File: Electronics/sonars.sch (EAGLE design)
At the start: 6 parts, among them X1 GLX-S-88M

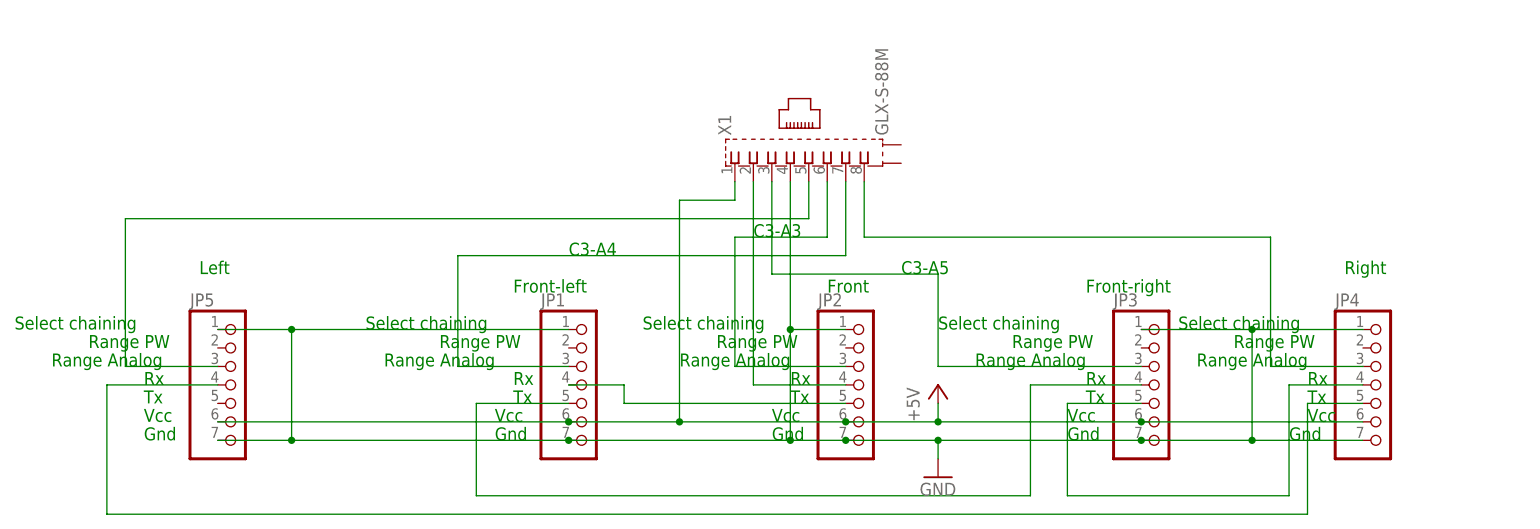
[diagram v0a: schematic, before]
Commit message: Parts match physical size
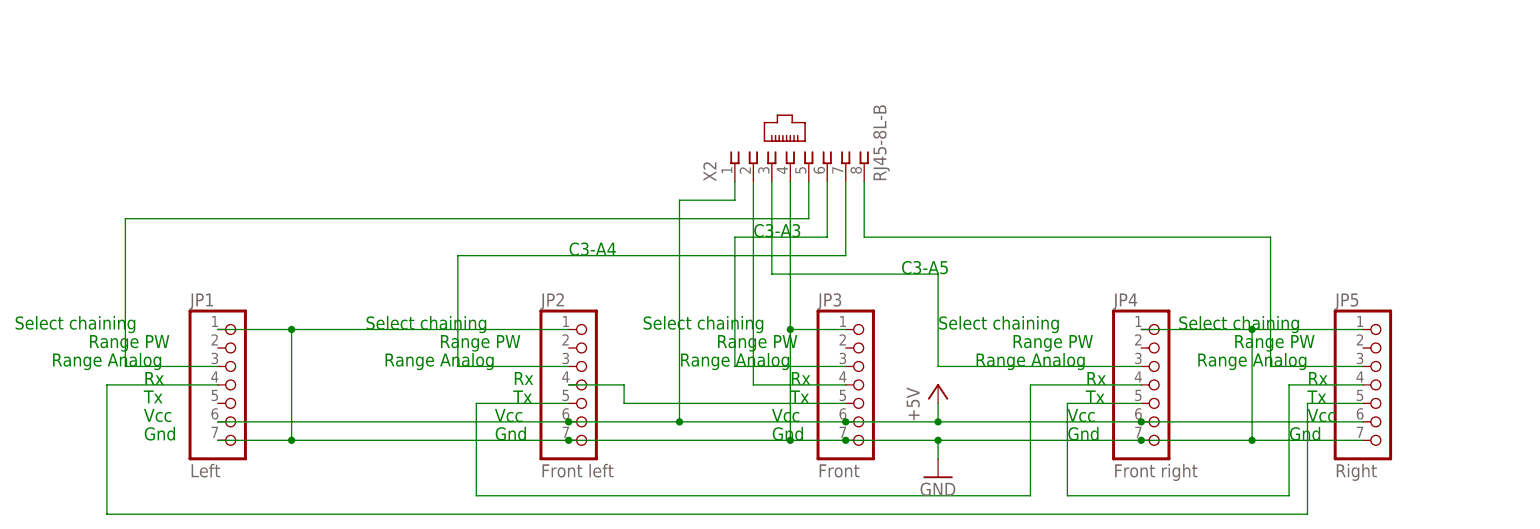
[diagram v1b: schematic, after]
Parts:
- removed X1: GLX-S-88M, con-kycon:GLX-S-88M
- added X2: RJ45-8L-B, con-tycoelectronics:RJ45-8L-B
- JP1: value (none) -> Left
- JP2: value (none) -> Front left
- JP3: value (none) -> Front
- JP4: value (none) -> Front right
- JP5: value (none) -> Right
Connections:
- net N$10 renamed FR>R
- removed net N$1: JP2.3, X1.6
- removed net N$11: JP4.3, X1.8
- removed net N$12: JP5.3, X1.5
- removed net N$2: JP1.3, X1.7
- removed net N$3: JP3.3, X1.3
- removed net N$5: JP2.4, X1.2
- removed net N$7: JP1.4, JP2.5
- removed net N$8: JP1.5, JP3.4
- removed net N$9: JP3.5, JP4.4
- new net CHN: JP3.4, X2.2
- new net F: JP3.3, X2.6
- new net F>FL: JP2.4, JP3.5
- new net FL: JP2.3, X2.7
- new net FL>FR: JP2.5, JP4.4
- new net FR: JP4.3, X2.3
- new net L: JP1.3, X2.5
- new net R: JP5.3, X2.8
- new net R>L: JP1.4, JP5.5
- net +5V: now also X2.1; no longer X1.1
- net GND: now also X2.4; no longer X1.4
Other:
- note removed: "Front"
- note removed: "Front-left"
- note removed: "Front-right"
- note removed: "Left"
- note removed: "Right"
- moved on the sheet: JP1, JP2, JP3, JP4, JP5

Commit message: Rear facing sonars; angles adjusted
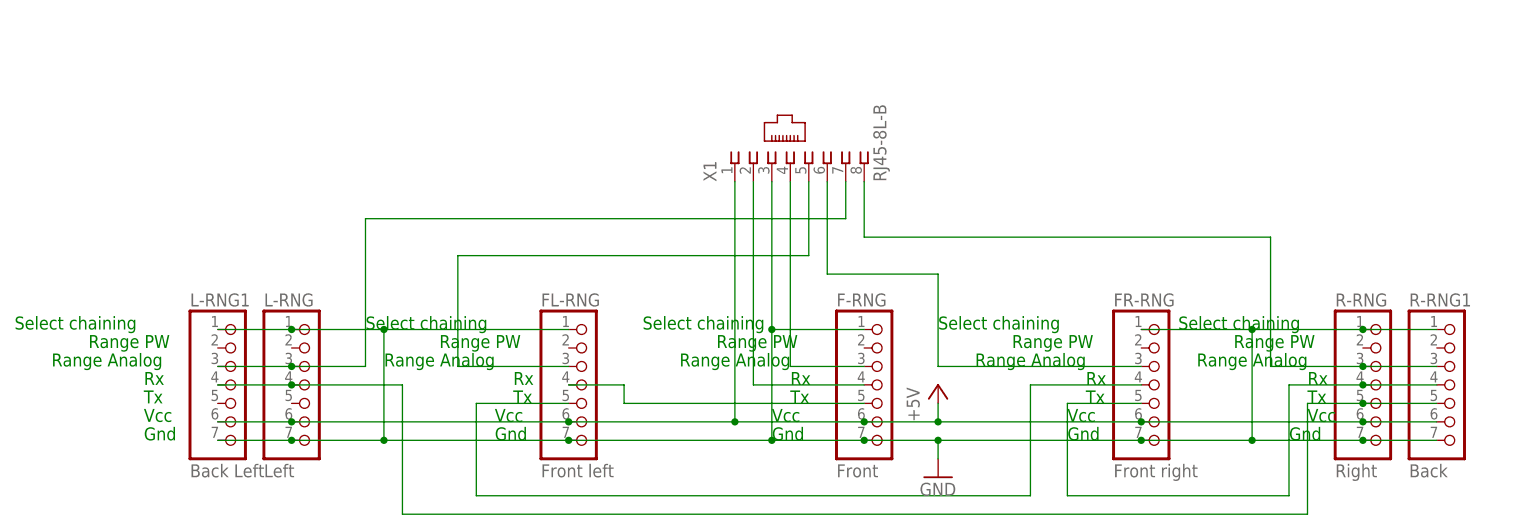
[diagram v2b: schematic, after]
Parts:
- removed JP3: Front, pinhead:PINHD-1X7
- added F-RNG: Front, pinhead:PINHD-1X7
- added L-RNG: Left, pinhead:PINHD-1X7
- added R-RNG1: Back, pinhead:PINHD-1X7
- L-RNG1: value Left -> Back Left
- renumbered JP1 to L-RNG1, JP2 to FL-RNG, JP4 to FR-RNG, JP5 to R-RNG, X2 to X1
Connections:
- removed net F: JP3.3, X1.6
- removed net FL: FL-RNG.3, X1.7
- removed net FR: FR-RNG.3, X1.3
- removed net L: L-RNG1.3, X1.5
- removed net R: R-RNG.3, X1.8
- new net FL_RNG: FL-RNG.3, X1.5
- new net FR_RNG: FR-RNG.3, X1.6
- new net F_RNG: F-RNG.3, X1.4
- new net L_RNG: L-RNG.3, L-RNG1.3, X1.7
- new net R_RNG: R-RNG.3, R-RNG1.3, X1.8
- net +5V: now also F-RNG.6, L-RNG.6, R-RNG1.6; no longer JP3.6
- net CHN: now also F-RNG.4; no longer JP3.4
- net F>FL: now also F-RNG.5; no longer JP3.5
- net FR>R: now also R-RNG1.4
- net GND: now also F-RNG.1, F-RNG.7, L-RNG.1, L-RNG.7, R-RNG1.1, R-RNG1.7, X1.3; no longer JP3.1, JP3.7, X1.4
- net R>L: now also L-RNG.4, R-RNG1.5
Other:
- note removed: "C3-A3"
- note removed: "C3-A4"
- note removed: "C3-A5"

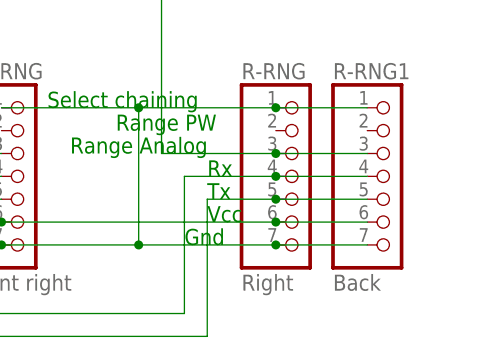
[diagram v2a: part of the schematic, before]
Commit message: Silkscreens; smaller sonar board
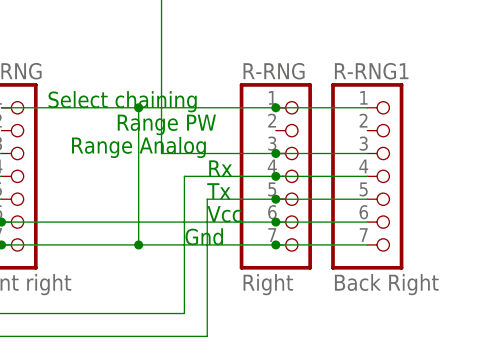
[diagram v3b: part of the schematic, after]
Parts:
- L-RNG1: value Back Left -> Back Left
- R-RNG1: value Back -> Back Right
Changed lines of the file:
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@@
 <part name="GND1" library="supply1" deviceset="GND" device=""/>
 <part name="X1" library="con-tycoelectronics" deviceset="RJ45" device="" technology="-8L-B"/>
-<part name="L-RNG1" library="pinhead" deviceset="PINHD-1X7" device="" value="Back Left"/>
-<part name="R-RNG1" library="pinhead" deviceset="PINHD-1X7" device="" value="Back"/>
+<part name="L-RNG1" library="pinhead" deviceset="PINHD-1X7" device="" value="        Back Left"/>
+<part name="R-RNG1" library="pinhead" deviceset="PINHD-1X7" device="" value="Back Right"/>
 </parts>
 <sheets>
